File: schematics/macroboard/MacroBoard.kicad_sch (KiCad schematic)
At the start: 82 parts, among them J1 USB4800-03-A_REVA, J2 Conn_01x08_Male, SW1 SW_Push, SW10 SW_Push, SW11 SW_Push, SW12 SW_Push, SW13 SW_Push, SW14 SW_Push, SW15 SW_Push, SW16 SW_Push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

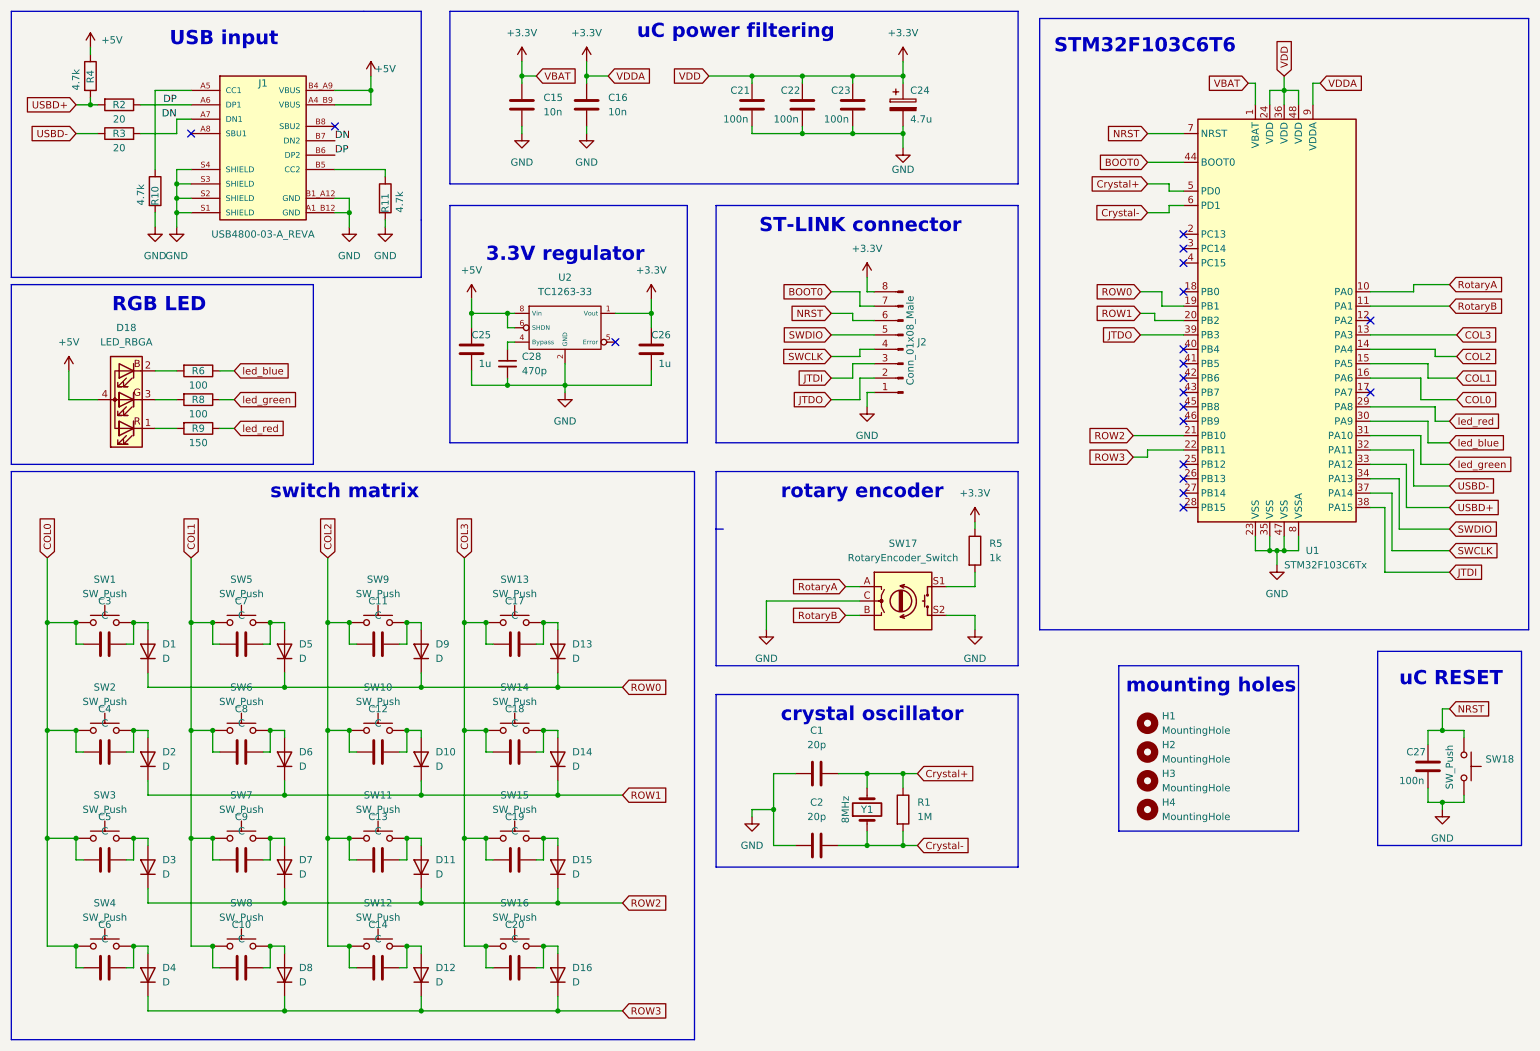
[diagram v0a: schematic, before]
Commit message: minor cleanup on schematic, hided value labels on switches on keyboard matrix for better readability
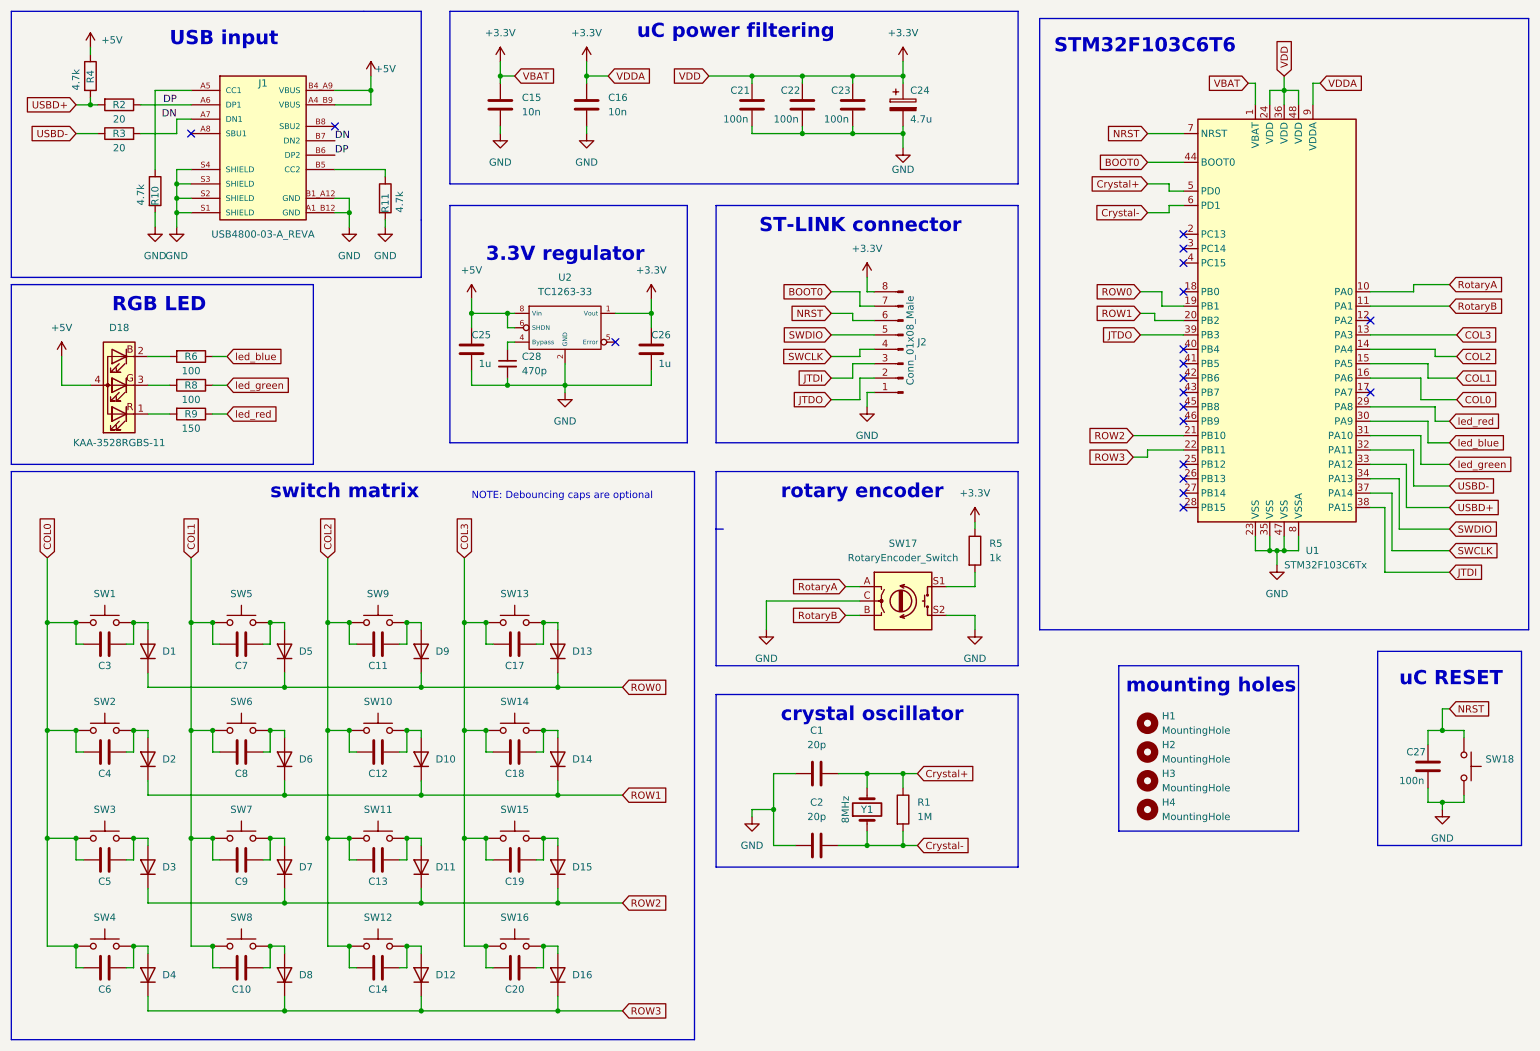
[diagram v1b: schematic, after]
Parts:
- D18: value LED_RBGA -> KAA-3528RGBS-11
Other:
- note added: "NOTE: Debouncing caps are optional"
- moved on the sheet: C15, D18, R6, R8, R9
